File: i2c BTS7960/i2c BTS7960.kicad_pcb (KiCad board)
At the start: 4 copper layers, 123.2 x 50.2 mm, 126 parts, among them J1 power in, J2 Conn_01x04, J3 jst, J4 Conn_01x04, J5 jst, J6 to qwiic breakout, J7 qwiic 1, J8 qwiic 2, U1 74AHC244, U10 BTS7960B, U11 BTS7960B, U12 ISO1540, U13 LD1117S33, U2 BTS7960B, U3 BTS7960B, U4 BTS7960B, U5 PCA9685, U6 BTS7960B, U7 74AHC244, U8 BTS7960B, U9 BTS7960B, U90 mp1584 dcdc

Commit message: motor driver and scale pcb gerbers
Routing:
- net Net-(D23-Pad1): track 60.0 -> 58.8 mm
- net GND: track 30.4 -> 31.5 mm
- net VCC: track 47.1 -> 46.2 mm
- net Net-(JP3-Pad2): track 25.3 -> 24.7 mm
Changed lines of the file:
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@@
       (layerselection 0x00010fc_ffffffff)
       (disableapertmacros false)
-      (usegerberextensions false)
-      (usegerberattributes true)
-      (usegerberadvancedattributes true)
-      (creategerberjobfile true)
+      (usegerberextensions true)
+      (usegerberattributes false)
+      (usegerberadvancedattributes false)
+      (creategerberjobfile false)
       (svguseinch false)
       (svgprecision 6)
@@
       (plotinvisibletext false)
       (sketchpadsonfab false)
-      (subtractmaskfromsilk false)
+      (subtractmaskfromsilk true)
       (outputformat 1)
       (mirror false)
-      (drillshape 1)
+      (drillshape 0)
       (scaleselection 1)
-      (outputdirectory "")
+      (outputdirectory "i2c BTS7960 gerbers/")
     )
   )
@@
       (effects (font (size 1 1) (thickness 0.15)))
     )
-    (fp_text value "330uF" (at 8.209677 -4.064) (layer "F.SilkS")
+    (fp_text value "330uF" (at 8.463677 -4.318) (layer "F.SilkS")
       (effects (font (size 1 1) (thickness 0.15)))
     )
@@
       (effects (font (size 1 1) (thickness 0.15)))
     )
-    (fp_text value "330uF" (at 7.447677 -4.826) (layer "F.SilkS")
+    (fp_text value "330uF" (at 7.701677 -5.334) (layer "F.SilkS")
       (effects (font (size 1 1) (thickness 0.15)))
     )
@@
     (fp_line (start 1.6 0.8) (end -1.6 0.8) (layer "F.Fab") (width 0.1))
     (fp_line (start -1.6 0.8) (end -1.6 -0.8) (layer "F.Fab") (width 0.1))
-    (pad "1" smd roundrect locked (at -1.475 0 270) (size 1.15 1.8) (layers "F.Cu" "F.Paste" "F.Mask") (roundrect_rratio 0.217391)
+    (pad "1" smd roundrect locked (at -1.475 0 270) (size 1.15 1.8) (layers "F.Cu" "F.Paste" "F.Mask") (roundrect_rratio 0.2173913043)
       (net 1 "+3V3") (pintype "passive"))
-    (pad "2" smd roundrect locked (at 1.475 0 270) (size 1.15 1.8) (layers "F.Cu" "F.Paste" "F.Mask") (roundrect_rratio 0.217391)
+    (pad "2" smd roundrect locked (at 1.475 0 270) (size 1.15 1.8) (layers "F.Cu" "F.Paste" "F.Mask") (roundrect_rratio 0.2173913043)
       (net 2 "GND") (pintype "passive"))
     (model "${KICAD6_3DMODEL_DIR}/Capacitor_SMD.3dshapes/C_1206_3216Metric.wrl"
@@
     (fp_line (start 1.6 -0.8) (end 1.6 0.8) (layer "F.Fab") (width 0.1))
     (fp_line (start 1.6 0.8) (end -1.6 0.8) (layer "F.Fab") (width 0.1))
-    (pad "1" smd roundrect locked (at -1.475 0 90) (size 1.15 1.8) (layers "F.Cu" "F.Paste" "F.Mask") (roundrect_rratio 0.217391)
+    (pad "1" smd roundrect locked (at -1.475 0 90) (size 1.15 1.8) (layers "F.Cu" "F.Paste" "F.Mask") (roundrect_rratio 0.2173913043)
       (net 3 "+5V") (pintype "passive"))
-    (pad "2" smd roundrect locked (at 1.475 0 90) (size 1.15 1.8) (layers "F.Cu" "F.Paste" "F.Mask") (roundrect_rratio 0.217391)
+    (pad "2" smd roundrect locked (at 1.475 0 90) (size 1.15 1.8) (layers "F.Cu" "F.Paste" "F.Mask") (roundrect_rratio 0.2173913043)
       (net 2 "GND") (pintype "passive"))
     (model "${KICAD6_3DMODEL_DIR}/Capacitor_SMD.3dshapes/C_1206_3216Metric.wrl"
@@
       (effects (font (size 0.4 0.4) (thickness 0.06)) (justify mirror))
     )
-    (fp_line (start -0.237258 -0.5225) (end 0.237258 -0.5225) (layer "B.SilkS") (width 0.12))
     (fp_line (start -0.237258 0.5225) (end 0.237258 0.5225) (layer "B.SilkS") (width 0.12))
+    (fp_line (start -0.237258 -0.5225) (end 0.237258 -0.5225) (layer "B.SilkS") (width 0.12))
     (fp_line (start 1.48 0.73) (end 1.48 -0.73) (layer "B.CrtYd") (width 0.05))
     (fp_line (start -1.48 -0.73) (end -1.48 0.73) (layer "B.CrtYd") (width 0.05))
-    (fp_line (start 1.48 -0.73) (end -1.48 -0.73) (layer "B.CrtYd") (width 0.05))
     (fp_line (start -1.48 0.73) (end 1.48 0.73) (layer "B.CrtYd") (width 0.05))
+    (fp_line (start 1.48 -0.73) (end -1.48 -0.73) (layer "B.CrtYd") (width 0.05))
     (fp_line (start -0.8 -0.4125) (end -0.8 0.4125) (layer "B.Fab") (width 0.1))
     (fp_line (start -0.8 0.4125) (end 0.8 0.4125) (layer "B.Fab") (width 0.1))
@@
   (segment (start 152.244812 87.84648) (end 145.00852 87.84648) (width 0.25) (layer "B.Cu") (net 2))
   (segment (start 162.213 94.649) (end 162.56 94.996) (width 0.25) (layer "B.Cu") (net 2))
+  (segment (start 162.56 94.996) (end 162.56 96.012) (width 0.25) (layer "B.Cu") (net 2))
   (segment (start 153.935 88.149) (end 153.681 88.149) (width 0.25) (layer "B.Cu") (net 2))
   (segment (start 153.322022 88.298022) (end 152.696354 88.298022) (width 0.25) (layer "B.Cu") (net 2))
@@
   (segment (start 135.675138 88.011) (end 135.193 88.011) (width 0.4) (layer "B.Cu") (net 5))
   (segment (start 127.45848 83.19948) (end 128.333 84.074) (width 0.4) (layer "B.Cu") (net 5))
-  (segment (start 130.6765 83.4325) (end 130.90952 83.19948) (width 0.4) (layer "B.Cu") (net 5))
   (segment (start 136.652 83.907862) (end 136.652 84.836) (width 0.4) (layer "B.Cu") (net 5))
   (segment (start 128.969 86.36) (end 128.969 84.137) (width 0.4) (layer "B.Cu") (net 5))
-  (segment (start 136.245618 83.50148) (end 136.652 83.907862) (width 0.4) (layer "B.Cu") (net 5))
   (segment (start 135.510627 82.766489) (end 131.342511 82.766489) (width 0.4) (layer "B.Cu") (net 5))
   (segment (start 136.652 83.907862) (end 135.510627 82.766489) (width 0.4) (layer "B.Cu") (net 5))
@@
   (segment (start 137.31348 129.52798) (end 138.113 130.3275) (width 0.25) (layer "F.Cu") (net 8))
   (segment (start 140.208 130.302) (end 141.983 128.527) (width 0.25) (layer "F.Cu") (net 8))
-  (segment (start 136.540039 124.317961) (end 135.270039 124.317961) (width 0.6) (layer "F.Cu") (net 8))
   (segment (start 108.458 115.57) (end 108.204 115.824) (width 0.6) (layer "F.Cu") (net 8))
   (segment (start 108.458 106.672) (end 108.458 115.57) (width 0.6) (layer "F.Cu") (net 8))
@@
   (segment (start 134.1375 84.328) (end 135.6615 82.804) (width 0.25) (layer "F.Cu") (net 21))
   (segment (start 134.049 84.328) (end 134.1375 84.328) (width 0.25) (layer "F.Cu") (net 21))
-  (segment (start 135.6615 82.804) (end 135.573 82.804) (width 0.25) (layer "F.Cu") (net 21))
   (segment (start 218.186 120.396) (end 219.6845 120.396) (width 0.25) (layer "F.Cu") (net 22))
   (segment (start 218.249 117.094) (end 219.6845 117.094) (width 0.25) (layer "F.Cu") (net 23))
@@
   (segment (start 125.86252 84.38648) (end 132.59544 84.38648) (width 0.25) (layer "F.Cu") (net 24))
   (segment (start 133.858 85.64904) (end 133.858 85.852) (width 0.25) (layer "F.Cu") (net 24))
-  (segment (start 115.316 86.614) (end 115.57 86.868) (width 0.25) (layer "F.Cu") (net 24))
   (segment (start 108.673 86.643928) (end 110.375488 84.94144) (width 0.25) (layer "F.Cu") (net 24))
   (segment (start 113.64344 84.94144) (end 115.316 86.614) (width 0.25) (layer "F.Cu") (net 24))
@@
   (segment (start 152.697009 90.39104) (end 156.570018 86.518031) (width 0.25) (layer "F.Cu") (net 30))
   (segment (start 152.697008 90.39104) (end 152.697009 90.39104) (width 0.25) (layer "F.Cu") (net 30))
-  (segment (start 152.4 90.39104) (end 152.697008 90.39104) (width 0.25) (layer "F.Cu") (net 30))
-  (segment (start 152.697008 90.39104) (end 152.913024 90.175024) (width 0.25) (layer "F.Cu") (net 30))
   (segment (start 146.812 84.216) (end 146.812 87.567) (width 0.25) (layer "F.Cu") (net 30))
   (segment (start 146.812 87.567) (end 147.257 87.567) (width 0.25) (layer "F.Cu") (net 30))
@@
         (xy 175.006 124.714)
         (xy 180.848 120.904)
-        (xy 180.848 108.712)
-        (xy 191.77 108.712)
+        (xy 180.848 109.22)
+        (xy 191.77 109.22)
       )
     )
@@
         (xy 146.812 120.65)
         (xy 133.604 130.048)
-        (xy 129.54 130.048)
-        (xy 129.54 125.222)
-        (xy 135.89 120.904)
-        (xy 135.89 108.966)
-        (xy 146.812 108.712)
+        (xy 129.794 130.048)
+        (xy 129.794 125.222)
+        (xy 136.144 120.904128)
+        (xy 136.149907 109.220128)
+        (xy 146.817907 109.219863)
       )
     )
@@
         (xy 119.38 125.222)
         (xy 114.046 120.65)
-        (xy 114.046 108.966)
-        (xy 124.46 108.966)
+        (xy 114.046 109.22)
+        (xy 124.46 109.22)
       )
     )
@@
         (xy 164.338 130.048)
         (xy 157.734 130.048)
-        (xy 147.32 120.65)
-        (xy 147.32 108.712)
-        (xy 158.496 108.712)
+        (xy 147.574 120.65)
+        (xy 147.574 109.22)
+        (xy 158.496 109.22)
       )
     )
@@
         (xy 164.846 124.46)
         (xy 159.004 120.142)
-        (xy 159.004 108.712)
-        (xy 169.418 108.712)
+        (xy 159.004 109.22)
+        (xy 169.418 109.22)
       )
     )
@@
     (polygon
       (pts
-        (xy 180.34 120.65)
-        (xy 174.498 124.46)
-        (xy 174.498 130.048)
+        (xy 180.086 120.65)
+        (xy 174.244 124.46)
+        (xy 174.244 130.048)
         (xy 169.926 130.048)
-        (xy 169.926 108.712)
-        (xy 180.34 108.712)
+        (xy 169.926 109.22)
+        (xy 180.086 109.22)
       )
     )
@@
         (xy 115.062 130.048)
         (xy 103.124 121.158)
-        (xy 103.124 108.966)
-        (xy 113.538 108.966)
+        (xy 103.124 109.22)
+        (xy 113.538 109.22)
       )
     )
@@
         (xy 129.032 124.968)
         (xy 129.032 130.048)
-        (xy 124.46 130.048)
-        (xy 124.46 124.968)
-        (xy 124.968 120.65)
-        (xy 124.968 108.966)
-        (xy 135.382 108.966)
+        (xy 124.714 130.048)
+        (xy 124.714 124.968)
+        (xy 125.222 120.65)
+        (xy 125.222 109.22)
+        (xy 135.382 109.22)
       )
     )

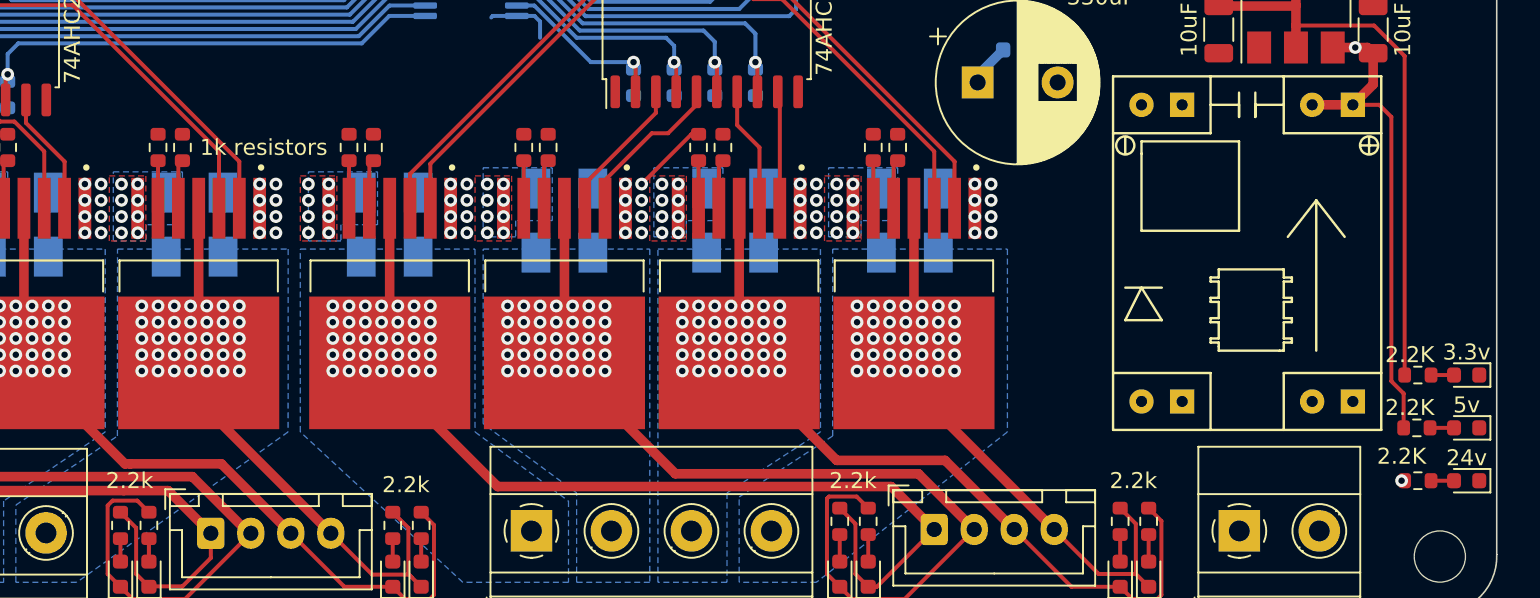
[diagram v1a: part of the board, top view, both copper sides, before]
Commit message: tweaked buck converter hole sizes and silk
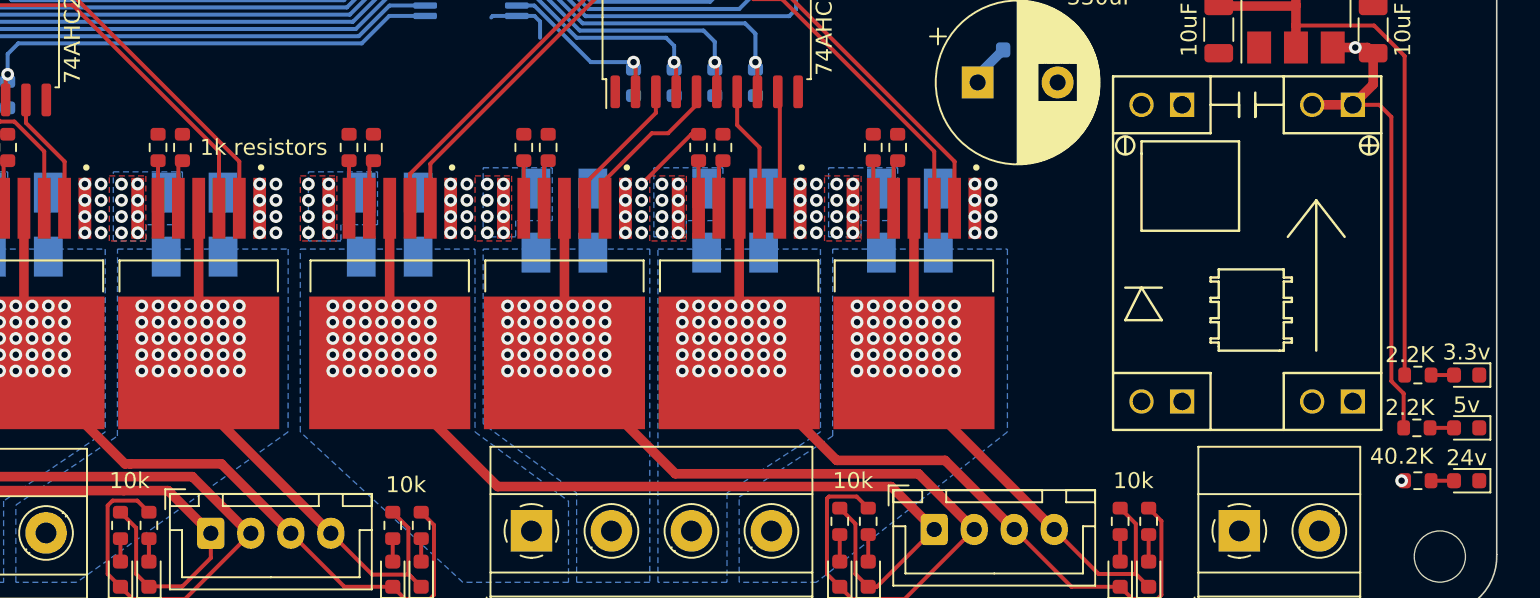
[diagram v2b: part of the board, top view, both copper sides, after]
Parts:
- R48: value 2.2K -> 40.2K
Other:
- board text removed: "2.2k"
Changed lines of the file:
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@@
       (effects (font (size 1 1) (thickness 0.15)))
     )
-    (fp_text value "2.2K" (at -1.016 -1.524) (layer "F.SilkS")
+    (fp_text value "40.2K" (at -1.016 -1.524) (layer "F.SilkS")
       (effects (font (size 1 1) (thickness 0.15)))
     )
@@
     (fp_circle (center 6.731 7.62) (end 7.239 7.874) (layer "F.SilkS") (width 0.15) (fill none))
     (fp_circle (center 6.731 -7.62) (end 7.239 -7.874) (layer "F.SilkS") (width 0.15) (fill none))
-    (pad "1" thru_hole rect (at -9.271 6.604 90) (size 1.524 1.524) (drill 0.7) (layers *.Cu *.Mask "F.SilkS")
+    (pad "1" thru_hole rect (at -9.271 6.604 90) (size 1.524 1.524) (drill 1.1) (layers *.Cu *.Mask "F.SilkS")
       (net 4 "+24V") (pinfunction "Pin_1") (pintype "passive"))
-    (pad "1" thru_hole circle (at -9.271 4.064 90) (size 1.524 1.524) (drill 0.7) (layers *.Cu *.Mask "F.SilkS")
+    (pad "1" thru_hole circle (at -9.271 4.064 90) (size 1.524 1.524) (drill 1.1) (layers *.Cu *.Mask "F.SilkS")
       (net 4 "+24V") (pinfunction "Pin_1") (pintype "passive"))
-    (pad "2" thru_hole rect (at -9.271 -4.064 90) (size 1.524 1.524) (drill 0.7) (layers *.Cu *.Mask "F.SilkS")
+    (pad "2" thru_hole rect (at -9.271 -4.064 90) (size 1.524 1.524) (drill 1.1) (layers *.Cu *.Mask "F.SilkS")
       (net 2 "GND") (pinfunction "Pin_2") (pintype "passive"))
-    (pad "2" thru_hole circle (at -9.271 -6.604 90) (size 1.524 1.524) (drill 0.7) (layers *.Cu *.Mask "F.SilkS")
+    (pad "2" thru_hole circle (at -9.271 -6.604 90) (size 1.524 1.524) (drill 1.1) (layers *.Cu *.Mask "F.SilkS")
       (net 2 "GND") (pinfunction "Pin_2") (pintype "passive"))
-    (pad "3" thru_hole rect (at 9.271 -4.064 90) (size 1.524 1.524) (drill 0.7) (layers *.Cu *.Mask "F.SilkS")
+    (pad "3" thru_hole rect (at 9.271 -4.064 90) (size 1.524 1.524) (drill 1.1) (layers *.Cu *.Mask "F.SilkS")
       (net 2 "GND") (pinfunction "Pin_3") (pintype "passive"))
-    (pad "3" thru_hole circle (at 9.271 -6.604 90) (size 1.524 1.524) (drill 0.7) (layers *.Cu *.Mask "F.SilkS")
+    (pad "3" thru_hole circle (at 9.271 -6.604 90) (size 1.524 1.524) (drill 1.1) (layers *.Cu *.Mask "F.SilkS")
       (net 2 "GND") (pinfunction "Pin_3") (pintype "passive"))
-    (pad "4" thru_hole circle (at 9.271 4.064 90) (size 1.524 1.524) (drill 0.7) (layers *.Cu *.Mask "F.SilkS")
+    (pad "4" thru_hole circle (at 9.271 4.064 90) (size 1.524 1.524) (drill 1.1) (layers *.Cu *.Mask "F.SilkS")
       (net 3 "+5V") (pinfunction "Pin_4") (pintype "passive"))
-    (pad "4" thru_hole rect (at 9.271 6.604 90) (size 1.524 1.524) (drill 0.7) (layers *.Cu *.Mask "F.SilkS")
+    (pad "4" thru_hole rect (at 9.271 6.604 90) (size 1.524 1.524) (drill 1.1) (layers *.Cu *.Mask "F.SilkS")
       (net 3 "+5V") (pinfunction "Pin_4") (pintype "passive"))
   )
@@
     (effects (font (size 1 1) (thickness 0.15)))
   )
-  (gr_text "2.2k" (at 154.178 123.952) (layer "F.SilkS")
+  (gr_text "10k" (at 154.178 123.952) (layer "F.SilkS")
     (effects (font (size 1 1) (thickness 0.15)))
   )
@@
     (effects (font (size 1 1) (thickness 0.15)))
   )
-  (gr_text "2.2k" (at 136.906 123.698) (layer "F.SilkS")
+  (gr_text "10k" (at 136.906 123.698) (layer "F.SilkS")
     (effects (font (size 1 1) (thickness 0.15)))
   )
-  (gr_text "2.2k" (at 182.118 123.698) (layer "F.SilkS")
+  (gr_text "10k" (at 182.118 123.698) (layer "F.SilkS")
     (effects (font (size 1 1) (thickness 0.15)))
   )
@@
     (effects (font (size 1 1) (thickness 0.15)))
   )
-  (gr_text "2.2k" (at 199.644 123.698) (layer "F.SilkS")
+  (gr_text "10k" (at 199.644 123.698) (layer "F.SilkS")
     (effects (font (size 1 1) (thickness 0.15)))
   )

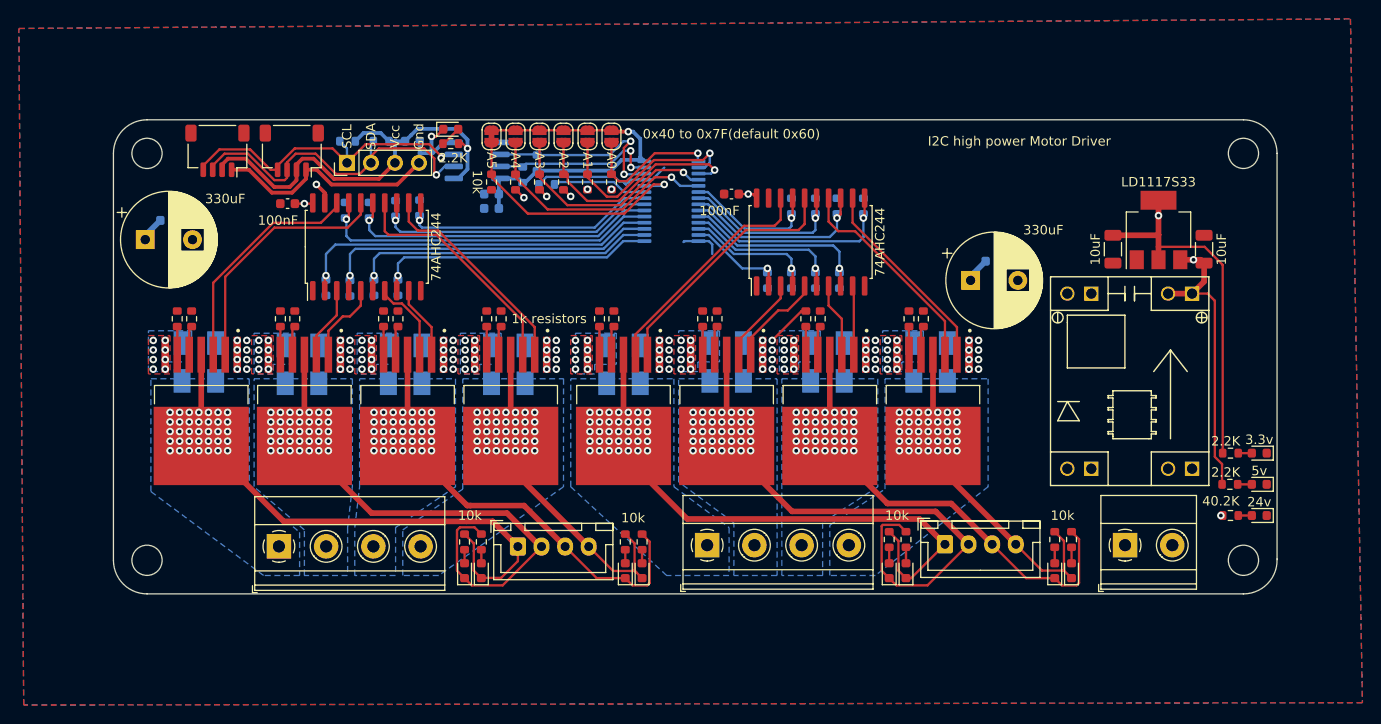
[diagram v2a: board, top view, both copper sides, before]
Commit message: reel detent added
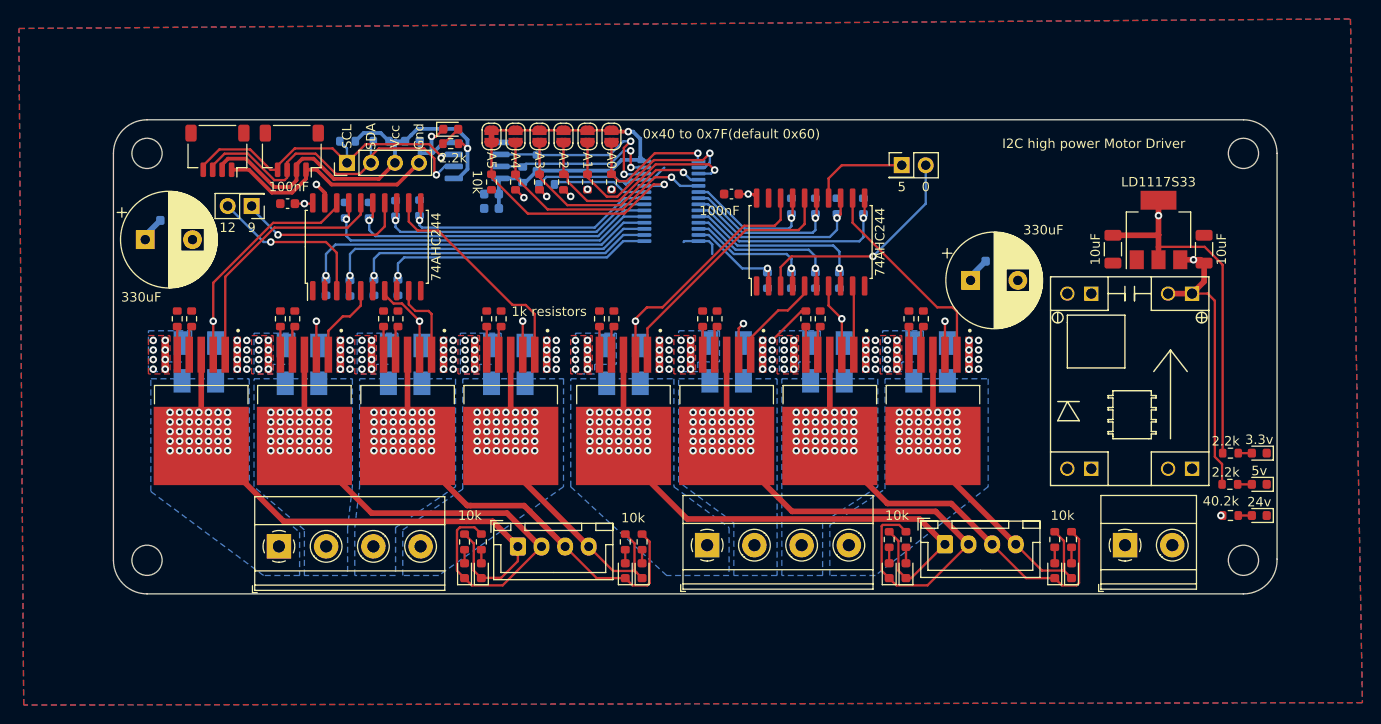
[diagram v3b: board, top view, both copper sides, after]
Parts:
- added G***: LOGO, Evan's misc parts:LC API, B.Cu at (207.5, 109.2)
- added J10: Conn_01x02, Connector_PinHeader_2.54mm:PinHeader_2x01_P2.54mm_Vertical, F.Cu at (113.8, 90.9)
- added J9: Conn_01x02, Connector_PinHeader_2.54mm:PinHeader_2x01_P2.54mm_Vertical, F.Cu at (182.6, 86.6)
- R17, R18, R19, R20, R31, R32, R42, R43: value 2.2k -> 10k
- R48: value 40.2K -> 40.2k
- R49, R52, R55: value 2.2K -> 2.2k
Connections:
- U11 pad 3: Net-(U11-Pad3) -> Net-(U10-Pad3)
- U3 pad 3: Net-(U1-Pad3) -> Net-(U1-Pad18)
- U6 pad 3: Net-(U1-Pad14) -> Net-(U1-Pad7)
- U7 pad 14: Net-(U11-Pad3) -> Net-(U7-Pad14)
- U7 pad 18: Net-(U7-Pad18) -> Net-(U9-Pad3)
- U8 pad 3: Net-(U7-Pad18) -> Net-(U9-Pad3)
- U9 pad 3: Net-(U7-Pad3) -> Net-(U9-Pad3)
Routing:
- net Net-(U9-Pad3): track 0.00 -> 38.9 mm, vias 0 -> 2
- net Net-(U11-Pad3): track 25.1 -> 0.00 mm
- net Net-(U7-Pad18): track 24.4 -> 0.00 mm
- net Net-(U7-Pad14): track 0.00 -> 18.4 mm, vias 0 -> 1
- net Net-(U1-Pad18): track 24.8 -> 40.8 mm, vias 0 -> 2
- net Net-(U1-Pad3): track 9.12 -> 24.2 mm, vias 0 -> 1
- net Net-(U1-Pad7): track 7.86 -> 22.4 mm, vias 0 -> 2
- net Net-(U10-Pad3): track 8.82 -> 23.3 mm, vias 0 -> 2
- net Net-(U1-Pad14): track 22.7 -> 10.4 mm
- net Net-(U7-Pad3): track 7.67 -> 17.6 mm, vias 0 -> 1
- net Net-(U1-Pad12): track 21.2 -> 22.1 mm
- net Net-(U11-Pad2): track 22.9 -> 23.7 mm
- net Net-(U10-Pad2): track 7.77 -> 8.58 mm
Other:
- board text added: "0"
- board text added: "12"
- board text added: "5"
- board text added: "9"
